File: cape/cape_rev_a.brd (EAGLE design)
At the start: 116.4 x 127.2 mm, 35 parts, among them IC1 MAX3042BEUE, IC10 MAX3042BEUE, IC11 MAX3042BEUE, IC12 MAX3042BEUE, IC13 MAX3042BEUE, IC14 MAX3042BEUE, IC15 MAX3042BEUE, IC16 MAX3042BEUE, IC2 MAX3042BEUE, IC3 MAX3042BEUE, IC4 MAX3042BEUE, IC5 MAX3042BEUE, IC6 MAX3042BEUE, IC7 MAX3042BEUE, IC8 MAX3042BEUE, IC9 MAX3042BEUE

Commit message: Mostly done with the receiver
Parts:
- moved U$3 26.7 mm to (9.83, 105.5), flipped to the bottom, turned to 180 degrees
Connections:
- new net CLOCK0: U$3.27
- new net CLOCK1: U$3.11
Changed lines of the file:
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@@
 <element name="C15" library="SparkFun-Passives" package="0603-CAP" value="0.1uF" x="73.9592" y="106" rot="R180"/>
 <element name="C16" library="SparkFun-Passives" package="0603-CAP" value="0.1uF" x="73.9846" y="112.8862" rot="R180"/>
-<element name="U$3" library="microbuilder" package="BEAGLEBONE_OUTLINE_DOCU" value="BEAGLEBONE_OUTLINEDOCU_OUTLINE" x="-14.619" y="94.765" rot="R270"/>
+<element name="U$3" library="microbuilder" package="BEAGLEBONE_OUTLINE_DOCU" value="BEAGLEBONE_OUTLINEDOCU_OUTLINE" x="9.8322" y="105.5256" rot="MR180"/>
 </elements>
 <signals>
@@
 <wire x1="92.237" y1="5.701" x2="82.0388" y2="13.0908" width="0" layer="19" extent="1-1"/>
 <wire x1="98.587" y1="6.463" x2="92.237" y2="5.701" width="0" layer="19" extent="1-1"/>
-<wire x1="60.311" y1="42.06" x2="73.1854" y2="43.0336" width="0" layer="19" extent="1-1"/>
-<wire x1="60.311" y1="44.6" x2="60.311" y2="42.06" width="0" layer="19" extent="1-1"/>
-<wire x1="57.771" y1="44.6" x2="60.311" y2="44.6" width="0" layer="19" extent="1-1"/>
-<wire x1="57.771" y1="42.06" x2="60.311" y2="42.06" width="0" layer="19" extent="1-1"/>
+<wire x1="62.5372" y1="30.5956" x2="73.1854" y2="43.0336" width="0" layer="19" extent="1-1"/>
+<wire x1="59.9972" y1="30.5956" x2="62.5372" y2="30.5956" width="0" layer="19" extent="1-1"/>
+<wire x1="59.9972" y1="33.1356" x2="59.9972" y2="30.5956" width="0" layer="19" extent="1-1"/>
+<wire x1="62.5372" y1="33.1356" x2="62.5372" y2="30.5956" width="0" layer="19" extent="1-1"/>
 <wire x1="112.303" y1="5.701" x2="98.587" y2="6.463" width="0" layer="19" extent="1-1"/>
-<wire x1="4.431" y1="44.6" x2="57.771" y2="44.6" width="0" layer="19" extent="1-1"/>
-<wire x1="4.431" y1="42.06" x2="4.431" y2="44.6" width="0" layer="19" extent="1-1"/>
-<wire x1="4.431" y1="90.32" x2="4.431" y2="44.6" width="0" layer="19" extent="1-1"/>
-<wire x1="4.431" y1="92.86" x2="4.431" y2="90.32" width="0" layer="19" extent="1-1"/>
+<wire x1="59.9972" y1="86.4756" x2="59.9972" y2="33.1356" width="0" layer="19" extent="1-1"/>
+<wire x1="62.5372" y1="86.4756" x2="59.9972" y2="86.4756" width="0" layer="19" extent="1-1"/>
+<wire x1="14.2772" y1="86.4756" x2="59.9972" y2="86.4756" width="0" layer="19" extent="1-1"/>
+<wire x1="11.7372" y1="86.4756" x2="14.2772" y2="86.4756" width="0" layer="19" extent="1-1"/>
 </signal>
 <signal name="VCC">
@@
 <contactref element="U$3" pad="49"/>
 <contactref element="U$3" pad="50"/>
-<wire x1="6.971" y1="42.06" x2="6.971" y2="44.6" width="0" layer="19" extent="1-1"/>
+<wire x1="62.5372" y1="83.9356" x2="59.9972" y2="83.9356" width="0" layer="19" extent="1-1"/>
 </signal>
 <signal name="VDD_5V">
 <contactref element="U$3" pad="51"/>
 <contactref element="U$3" pad="52"/>
-<wire x1="9.511" y1="42.06" x2="9.511" y2="44.6" width="0" layer="19" extent="1-1"/>
+<wire x1="62.5372" y1="81.3956" x2="59.9972" y2="81.3956" width="0" layer="19" extent="1-1"/>
 </signal>
 <signal name="SYS_5V">
 <contactref element="U$3" pad="53"/>
 <contactref element="U$3" pad="54"/>
-<wire x1="12.051" y1="42.06" x2="12.051" y2="44.6" width="0" layer="19" extent="1-1"/>
+<wire x1="62.5372" y1="78.8556" x2="59.9972" y2="78.8556" width="0" layer="19" extent="1-1"/>
 </signal>
 <signal name="VDD_ADC">
@@
 <wire x1="76.2032" y1="9.1908" x2="76.2032" y2="16.0702" width="0" layer="19" extent="1-1"/>
 </signal>
+<signal name="CLOCK1">
+<contactref element="U$3" pad="11"/>
+</signal>
+<signal name="CLOCK0">
+<contactref element="U$3" pad="27"/>
+</signal>
 </signals>

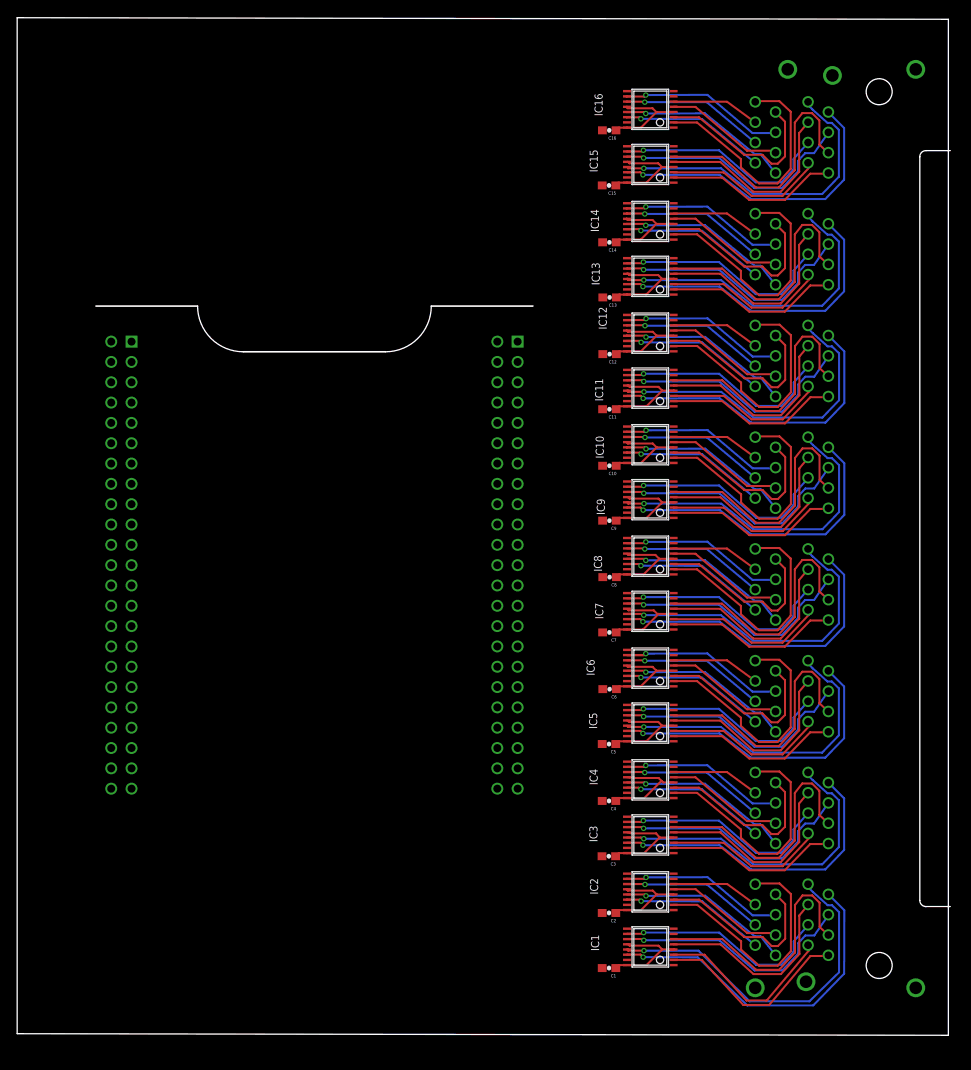
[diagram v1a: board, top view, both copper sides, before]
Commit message: Almost done with cape routing
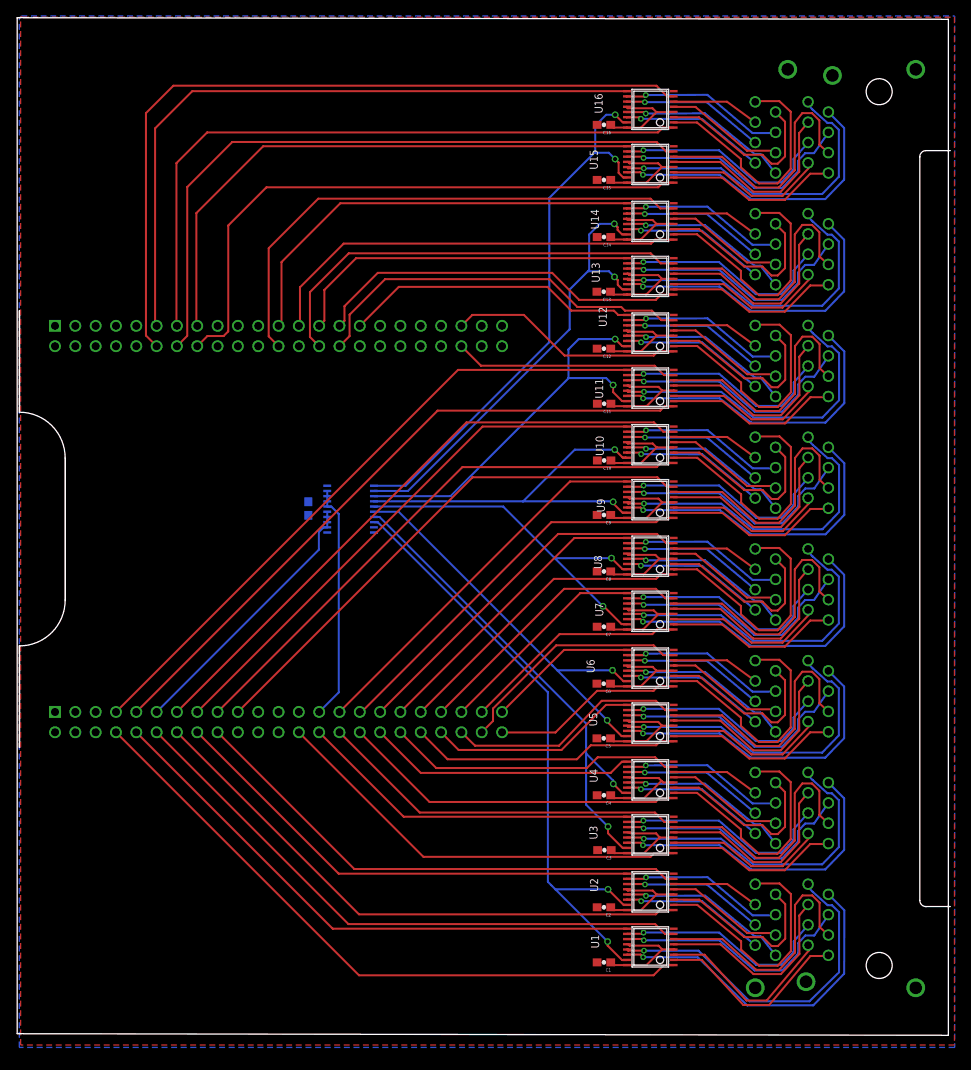
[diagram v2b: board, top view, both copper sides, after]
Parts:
- added C17: 0.1uF, SparkFun-Passives:0603-CAP
- added U17: SN74LV245, microbuilder:TSSOP20
- moved U$3 73.9 mm to (-14.3, 35.7), turned to 90 degrees
- moved C13 1.02 mm to (73.3, 92.7)
- moved C6 1.01 mm to (73.3, 43.7)
- moved C8 1.01 mm to (73.3, 57.7)
- moved C7 0.99 mm to (73.3, 50.8)
- moved C12 0.99 mm to (73.3, 85.6)
- moved C9 0.99 mm to (73.3, 64.8)
- moved C5 0.97 mm to (73.3, 36.9)
- moved C4 0.95 mm to (73.3, 29.8)
- moved C1 0.95 mm to (73.3, 8.88)
- moved C2 0.95 mm to (73.3, 15.8)
- moved C11 0.95 mm to (73.3, 78.7)
- moved C14 0.95 mm to (73.3, 99.5)
- moved C16 0.95 mm to (73.3, 113.6)
- moved C3 0.94 mm to (73.4, 22.9)
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- renumbered IC1 to U1, IC10 to U10, IC11 to U11, IC12 to U12, IC13 to U13, IC14 to U14, IC15 to U15, IC16 to U16, IC2 to U2, IC3 to U3, IC4 to U4, IC5 to U5, IC6 to U6, IC7 to U7, IC8 to U8, IC9 to U9
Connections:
- removed net CLOCK0: U$3.27
- removed net CLOCK1: U$3.11
- removed net N$1: U1.1, U10.1, U11.1, U12.1, U13.1, U14.1, U15.1, U16.1, U2.1, U3.1, U4.1, U5.1, U6.1, U7.1, U8.1, U9.1
- removed net N$2: U1.7, U10.7, U11.7, U12.7, U13.7, U14.7, U15.7, U16.7, U2.7, U3.7, U4.7, U5.7, U6.7, U7.7, U8.7, U9.7
- removed net N$3: U1.9, U10.9, U11.9, U12.9, U13.9, U14.9, U15.9, U16.9, U2.9, U3.9, U4.9, U5.9, U6.9, U7.9, U8.9, U9.9
- removed net N$4: U1.15, U10.15, U11.15, U12.15, U13.15, U14.15, U15.15, U16.15, U2.15, U3.15, U4.15, U5.15, U6.15, U7.15, U8.15, U9.15
- removed net VDD_5V: U$3.51, U$3.52
- new net CK0-1: U1.15, U17.18, U2.15
- new net CK0-2: U17.17, U3.15, U4.15
- new net CK0-3: U17.16, U5.15, U6.15
- new net CK0-4: U17.15, U7.15, U8.15
- new net CK1-1: U10.15, U17.14, U9.15
- new net CK1-2: U11.15, U12.15, U17.13
- new net CK1-3: U13.15, U14.15, U17.12
- new net CK1-4: U15.15, U16.15, U17.11
- new net PRU0: U$3.11, U17.2, U17.3, U17.4, U17.5
- new net PRU1: U$3.27, U17.6, U17.7, U17.8, U17.9
- new net S0: U$3.8, U1.1
- new net S1: U$3.12, U1.7
- new net S10: U$3.36, U4.7
- new net S11: U$3.34, U4.9
- new net S12: U$3.38, U5.1
- new net S13: U$3.42, U5.7
- new net S14: U$3.40, U5.9
- new net S15: U$3.46, U6.1
- new net S16: U$3.44, U6.7
- new net S17: U$3.45, U6.9
- new net S18: U$3.43, U7.1
- new net S19: U$3.39, U7.7
- new net S2: U$3.10, U1.9
- new net S20: U$3.41, U7.9
- new net S21: U$3.37, U8.1
- new net S22: U$3.33, U8.7
- new net S23: U$3.35, U8.9
- new net S24: U$3.31, U9.1
- new net S25: U$3.19, U9.7
- new net S26: U$3.29, U9.9
- new net S27: U$3.17, U10.1
- new net S28: U$3.13, U10.7
- new net S29: U$3.15, U10.9
- new net S3: U$3.14, U2.1
- new net S30: U$3.9, U11.1
- new net S31: U$3.88, U11.7
- new net S32: U$3.7, U11.9
- new net S33: U$3.87, U12.1
- new net S34: U$3.76, U12.7
- new net S35: U$3.77, U12.9
- new net S36: U$3.75, U13.1
- new net S37: U$3.74, U13.7
- new net S38: U$3.73, U13.9
- new net S39: U$3.71, U14.1
- new net S4: U$3.18, U2.7
- new net S40: U$3.70, U14.7
- new net S41: U$3.69, U14.9
- new net S42: U$3.62, U15.1
- new net S43: U$3.60, U15.7
- new net S44: U$3.61, U15.9
- new net S45: U$3.59, U16.1
- new net S46: U$3.58, U16.7
- new net S47: U$3.57, U16.9
- new net S5: U$3.16, U2.9
- new net S6: U$3.26, U3.1
- new net S7: U$3.30, U3.7
- new net S8: U$3.28, U3.9
- new net S9: U$3.32, U4.1
- net GND: now also C17.2, U17.10, U17.19
- net VCC: now also C17.1, U$3.51, U$3.52, U17.1, U17.20
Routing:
- net S46: track 0.00 -> 97.6 mm
- net S47: track 0.00 -> 85.7 mm
- net S45: track 0.00 -> 84.4 mm
- net S43: track 0.00 -> 84.0 mm
- net S30: track 0.00 -> 83.0 mm
- net S0: track 0.00 -> 82.8 mm
- net S32: track 0.00 -> 81.6 mm
- net CK0-1: track 0.00 -> 78.2 mm, vias 0 -> 2
- net S28: track 0.00 -> 77.6 mm
- net S42: track 0.00 -> 75.8 mm
- net S1: track 0.00 -> 75.1 mm
- net S3: track 0.00 -> 71.7 mm
- net S2: track 0.00 -> 71.5 mm
- net S44: track 0.00 -> 71.4 mm
- net S27: track 0.00 -> 69.9 mm
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- added copper zone on layer 1, net GND
- added copper zone on layer 16, net VCC

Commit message: Cape rev a
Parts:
- moved C17 8.94 mm to (43.4, 60.1), turned to 0 degrees
- moved U12 0.88 mm to (78.8, 86.7)
- moved C4 0.88 mm to (73.0, 29.0)
- moved C5 0.88 mm to (73.0, 36.1)
- moved C6 0.88 mm to (73.0, 42.9)
- moved C7 0.88 mm to (73.0, 50.0)
- moved C8 0.88 mm to (73.0, 56.9)
- moved C2 0.88 mm to (73.0, 15.0)
- moved U$2 0.88 mm to (101.1, 8.95)
- moved U$3 0.88 mm to (-14.7, 34.9)
- moved C1 0.88 mm to (73.0, 8.07)
- moved C3 0.88 mm to (73.1, 22.1)
- moved FRAME1 0.88 mm to (0.05, 24.0)
- moved U5 0.88 mm to (78.8, 38.0)
- moved U7 0.88 mm to (78.8, 52.0)
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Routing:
- net VCC: track 211.9 -> 270.9 mm, vias 0 -> 16
- net GND: track 0.00 -> 27.0 mm, vias 0 -> 5
- net CK1-4: track 69.8 -> 80.6 mm
- net CK1-3: track 57.9 -> 63.6 mm
- net S45: track 84.4 -> 87.2 mm
- net S44: track 71.4 -> 73.1 mm
- net S43: track 84.0 -> 85.8 mm
- net S39: track 54.1 -> 55.3 mm
- net CK1-2: track 51.3 -> 51.9 mm
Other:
- board size 116.4 x 127.2 mm -> 116.1 x 124.1 mm
- board text added: "1"
- board text added: "10"
- board text added: "11"
- board text added: "12"
- board text added: "13"
- board text added: "14"
- board text added: "15"
- board text added: "16"
- board text added: "2"
- board text added: "2016"
- board text added: "3"
- board text added: "4"
- board text added: "5"
- board text added: "6"
- board text added: "7"
- board text added: "8"
- board text added: "9"
- board text added: "Designed by"
- board text added: "Rev. A"
- board text added: "Shlomo Zippel"
